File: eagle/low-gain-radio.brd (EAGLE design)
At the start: 99 x 100 mm, 109 parts, among them Y1 32MHz

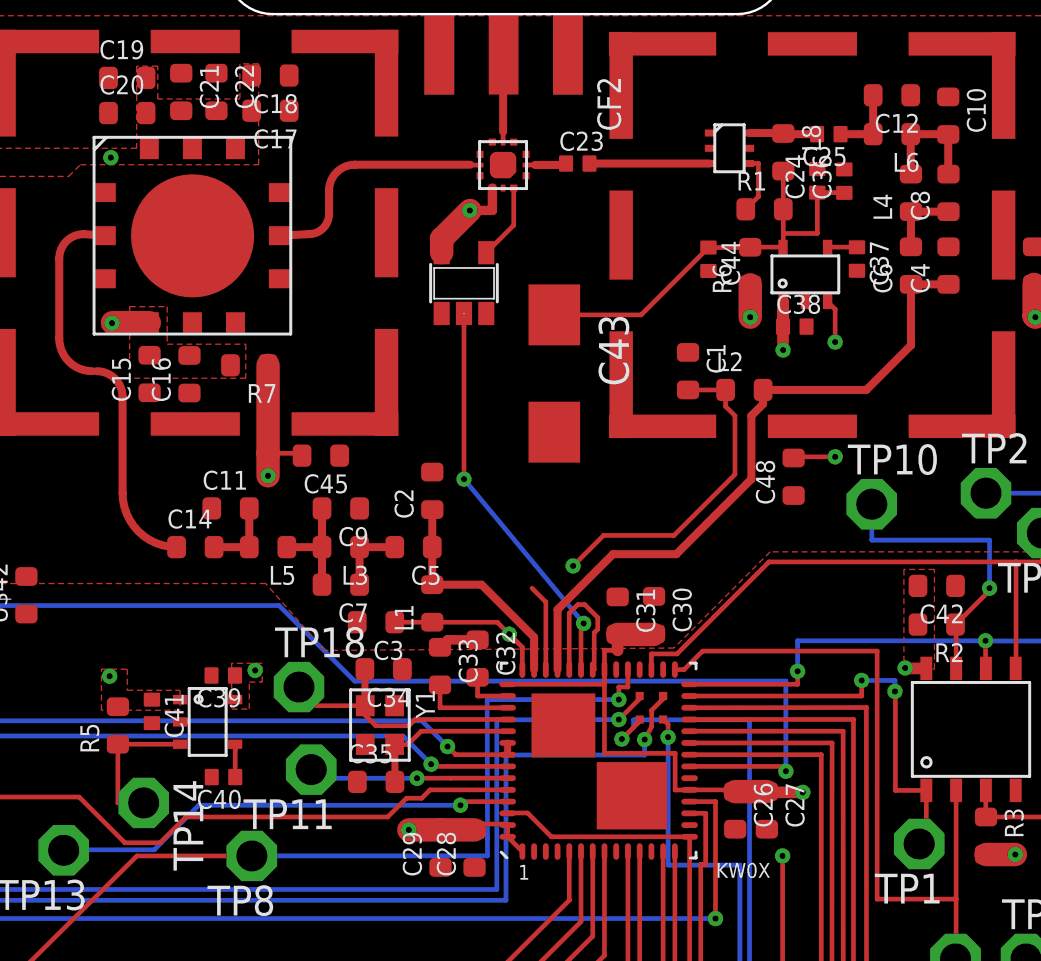
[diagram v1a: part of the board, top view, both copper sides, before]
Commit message: Fixed some part sizes. I'm not gonna talk about it since Andrew will surely fire me.
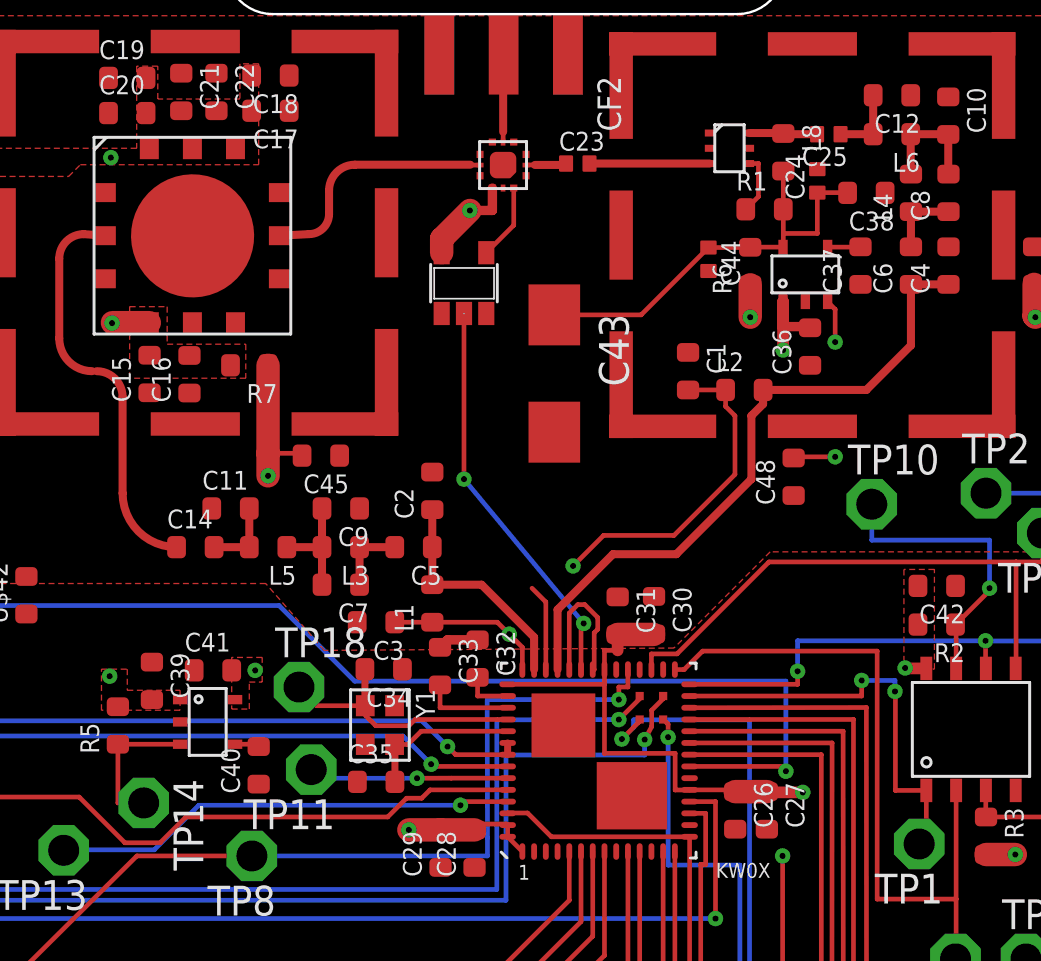
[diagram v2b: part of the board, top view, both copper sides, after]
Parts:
- C36, C39: value 2.2uF -> 1uF; device rcl_custom:.0402-B-NOSILK -> rcl_custom:.0603-B-NOSILK
- C37, C40: device rcl_custom:.0402-B-NOSILK -> rcl_custom:.0603-B-NOSILK
- C38: value 1uF -> 2.2nF; device rcl_custom:.0402-B-NOSILK -> rcl_custom:.0603-B-NOSILK
- C41: value 1uF -> 2.2uF; device rcl_custom:.0402-B-NOSILK -> rcl_custom:.0603-B-NOSILK
- moved C36 7.20 mm to (85.1, 76.0)
- moved C38 6.46 mm to (87.5, 82.5), turned to 180 degrees
- moved C41 3.13 mm to (59.6, 62.1), turned to 0 degrees
- moved C39 3.05 mm to (57.0, 61.7), turned to 270 degrees
- moved C40 1.58 mm to (61.6, 58.1), turned to 90 degrees
- moved C37 0.32 mm to (87.2, 79.4), turned to 90 degrees
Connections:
- net 3.3V: now also C41.2; no longer C39.1
- net GND: now also C36.1, C37.1, C38.1, C39.1, C40.1, C41.1; no longer C36.2, C37.2, C38.2, C39.2, C40.2, C41.2
- net N$1: now also C37.2; no longer C37.1
- net N$13: now also C40.2; no longer C40.1
- net V+: now also C36.2, C39.2; no longer C38.1, C41.1
- net VBIAS: now also C38.2; no longer C36.1
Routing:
- net V+: track 126.4 -> 127.6 mm
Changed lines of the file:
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@@
 <element name="C13" library="rcl_custom" package=".0603-B-NOSILK" value="10uF" x="45.65" y="81.85" rot="R180"/>
 <element name="C46" library="rcl_custom" package=".0603-B-NOSILK" value="10uF" x="48.8" y="84.6" rot="R270"/>
-<element name="C36" library="rcl_custom" package=".0402-B-NOSILK" value="2.2uF" x="86.56" y="83" rot="R90"/>
-<element name="C37" library="rcl_custom" package=".0402-B-NOSILK" value="10nF" x="87.1" y="79.68" rot="R270"/>
-<element name="C38" library="rcl_custom" package=".0402-B-NOSILK" value="1uF" x="84.45" y="76.8"/>
 <element name="U$8" library="psas_c3_team05" package="AAT3215" value="AAT3215" x="59.4" y="60.05" rot="R90">
 <attribute name="MFN" value="Skyworks" x="59.4" y="60.05" size="1.778" layer="27" rot="R90" display="off"/>
 <attribute name="MFN-PN" value="AAT3215" x="59.4" y="60.05" size="1.778" layer="27" rot="R90" display="off"/>
 </element>
-<element name="C39" library="rcl_custom" package=".0402-B-NOSILK" value="2.2uF" x="60.09" y="61.93" rot="R180"/>
-<element name="C40" library="rcl_custom" package=".0402-B-NOSILK" value="10nF" x="60.1" y="57.6" rot="R180"/>
-<element name="C41" library="rcl_custom" package=".0402-B-NOSILK" value="1uF" x="57.05" y="60.4" rot="R270"/>
 <element name="TP1" library="testpad" package="P1-13" value="TPSPAD1-13" x="89.75" y="54.75" rot="R180">
 <attribute name="TP_SIGNAL_NAME" value="" x="89.75" y="54.75" size="1.778" layer="27" rot="R180" display="off"/>
@@
 <element name="C48" library="rcl_custom" package=".0603-B-NOSILK" value="100nF" x="84.4" y="70.4" rot="R90"/>
 <element name="U$42" library="psas_c3_team05" package=".0603-B-NOSILK" value="742792651" x="51.7" y="65.35" rot="R90"/>
+<element name="C39" library="rcl_custom" package=".0603-B-NOSILK" value="1uF" x="57.05" y="61.7" rot="R270"/>
+<element name="C40" library="rcl_custom" package=".0603-B-NOSILK" value="10nF" x="61.6" y="58.1" rot="R90"/>
+<element name="C41" library="rcl_custom" package=".0603-B-NOSILK" value="2.2uF" x="59.65" y="62.15"/>
+<element name="C36" library="rcl_custom" package=".0603-B-NOSILK" value="1uF" x="85.1" y="75.95" rot="R90"/>
+<element name="C37" library="rcl_custom" package=".0603-B-NOSILK" value="10nF" x="87.25" y="79.4" rot="R90"/>
+<element name="C38" library="rcl_custom" package=".0603-B-NOSILK" value="2.2nF" x="87.5" y="82.5" rot="R180"/>
 </elements>
 <signals>
@@
 <contactref element="C29" pad="1"/>
 <contactref element="U$8" pad="2"/>
-<contactref element="C41" pad="2"/>
-<contactref element="C39" pad="2"/>
-<contactref element="C40" pad="2"/>
 <contactref element="U$1" pad="4"/>
 <contactref element="TRSWITCH" pad="11"/>
 <contactref element="U$7" pad="2"/>
-<contactref element="C38" pad="2"/>
-<contactref element="C36" pad="2"/>
-<contactref element="C37" pad="2"/>
 <contactref element="C42" pad="1"/>
 <contactref element="KW0X" pad="2"/>
@@
 <contactref element="LED3" pad="K"/>
 <contactref element="U$42" pad="1"/>
-<wire x1="87.1" y1="79.18" x2="86.56" y2="83.5" width="0" layer="19" extent="1-1"/>
-<wire x1="84.899" y1="77.858" x2="87.1" y2="79.18" width="0" layer="19" extent="1-1"/>
-<wire x1="84.95" y1="76.8" x2="84.899" y2="77.858" width="0" layer="19" extent="1-1"/>
-<wire x1="80.8275" y1="85.05" x2="86.56" y2="83.5" width="0" layer="19" extent="1-1"/>
-<wire x1="84.4" y1="69.6" x2="84.95" y2="76.8" width="0" layer="19" extent="1-1"/>
+<contactref element="C39" pad="1"/>
+<contactref element="C40" pad="1"/>
+<contactref element="C41" pad="1"/>
+<contactref element="C36" pad="1"/>
+<contactref element="C37" pad="1"/>
+<contactref element="C38" pad="1"/>
+<wire x1="87.25" y1="78.6" x2="88.3" y2="82.5" width="0" layer="19" extent="1-1"/>
+<wire x1="84.899" y1="77.858" x2="87.25" y2="78.6" width="0" layer="19" extent="1-1"/>
+<wire x1="85.1" y1="75.15" x2="84.899" y2="77.858" width="0" layer="19" extent="1-1"/>
+<wire x1="84.4" y1="69.6" x2="85.1" y2="75.15" width="0" layer="19" extent="1-1"/>
+<wire x1="80.8275" y1="85.05" x2="88.3" y2="82.5" width="0" layer="19" extent="1-1"/>
 <wire x1="91.3" y1="65.75" x2="84.4" y2="69.6" width="0" layer="19" extent="1-1"/>
 <wire x1="93.865" y1="57.032" x2="91.3" y2="65.75" width="0" layer="19" extent="1-1"/>
-<wire x1="57.05" y1="59.9" x2="58.258" y2="59.951" width="0" layer="19" extent="1-1"/>
+<wire x1="58.258" y1="59.951" x2="58.85" y2="62.15" width="0" layer="19" extent="1-1"/>
 <wire x1="69.35" y1="53.75" x2="65.8079125" y2="57.39725625" width="0" layer="19" extent="1-1"/>
 <wire x1="73.338371875" y1="54.427225" x2="70.8" y2="53.75" width="0" layer="19" extent="1-1"/>
@@
 <contactref element="U$9" pad="6"/>
 <contactref element="C13" pad="2"/>
-<contactref element="C38" pad="1"/>
-<contactref element="C41" pad="1"/>
 <contactref element="U$8" pad="1"/>
 <contactref element="U$7" pad="1"/>
@@
 <via x="44.85" y="80.45" extent="1-16" drill="0.254"/>
 <wire x1="83.949" y1="77.858" x2="83.949" y2="76.801" width="0.5" layer="1"/>
-<wire x1="83.949" y1="76.801" x2="83.95" y2="76.8" width="0.5" layer="1"/>
-<wire x1="83.949" y1="77.858" x2="83.949" y2="75.801" width="0.5" layer="1"/>
+<wire x1="83.949" y1="77.858" x2="83.949" y2="76.8" width="0.5" layer="1"/>
+<wire x1="83.949" y1="76.8" x2="83.949" y2="75.801" width="0.5" layer="1"/>
 <wire x1="83.949" y1="75.801" x2="83.95" y2="75.8" width="0.5" layer="1"/>
 <via x="83.95" y="75.8" extent="1-16" drill="0.254"/>
@@
 <wire x1="57.95" y1="71.9" x2="57.95" y2="70.85" width="1" layer="15"/>
 <wire x1="57.95" y1="70.85" x2="58.05" y2="70.85" width="1" layer="15"/>
+<contactref element="C39" pad="2"/>
+<contactref element="C36" pad="2"/>
+<wire x1="85.1" y1="76.75" x2="85.1" y2="76.8" width="0.2" layer="1"/>
+<wire x1="85.1" y1="76.8" x2="83.949" y2="76.8" width="0.4" layer="1"/>
 </signal>
 <signal name="SWD_DIO">
@@
 <contactref element="R2" pad="2"/>
 <contactref element="U$8" pad="5"/>
-<contactref element="C39" pad="1"/>
 <contactref element="R3" pad="2"/>
 <contactref element="R8" pad="2"/>
@@
 <via x="68" y="55.35" extent="1-16" drill="0.254"/>
 <polygon width="0.2" layer="1" thermals="no">
-<vertex x="60.45" y="62.45"/>
+<vertex x="60.45" y="62.7"/>
 <vertex x="60.45" y="60.5"/>
 <vertex x="61.2" y="60.5"/>
 <vertex x="61.2" y="61.65"/>
 <vertex x="61.75" y="61.65"/>
-<vertex x="61.75" y="62.45"/>
+<vertex x="61.75" y="62.7"/>
 </polygon>
 <via x="61.45" y="62.15" extent="1-16" drill="0.254"/>
@@
 <wire x1="72.165596875" y1="55.6" x2="71.05" y2="55.6" width="0.2" layer="1"/>
 <wire x1="71.05" y1="55.6" x2="70.8" y2="55.35" width="0.2" layer="1"/>
+<contactref element="C41" pad="2"/>
 </signal>
 <signal name="N$7">
@@
 </signal>
 <signal name="N$1">
-<contactref element="C37" pad="1"/>
 <contactref element="U$7" pad="4"/>
 <wire x1="85.849" y1="80.188" x2="87.1" y2="80.188" width="0.2" layer="1"/>
-<wire x1="87.1" y1="80.188" x2="87.1" y2="80.18" width="0.2" layer="1"/>
+<contactref element="C37" pad="2"/>
+<wire x1="87.1" y1="80.188" x2="87.25" y2="80.2" width="0" layer="19" extent="1-1"/>
 </signal>
 <signal name="PA_EN">
@@
 <signal name="N$13">
 <contactref element="U$8" pad="4"/>
-<contactref element="C40" pad="1"/>
-<wire x1="60.588" y1="59.001" x2="60.6" y2="58.775" width="0.2" layer="1"/>
-<wire x1="60.6" y1="58.775" x2="60.6" y2="57.6" width="0.2" layer="1"/>
+<contactref element="C40" pad="2"/>
+<wire x1="60.588" y1="59.001" x2="61.5" y2="59.001" width="0.2" layer="1"/>
+<wire x1="61.5" y1="59.001" x2="61.6" y2="58.9" width="0.4064" layer="1"/>
 </signal>
 <signal name="VBIAS">
 <contactref element="R1" pad="2"/>
-<contactref element="C36" pad="1"/>
 <contactref element="C24" pad="1"/>
 <contactref element="C43" pad="+"/>
@@
 <wire x1="83.96" y1="80.77" x2="83.96" y2="81.8" width="0.2" layer="1"/>
 <wire x1="83.96" y1="81.8" x2="83.96" y2="83.43" width="0.2" layer="1"/>
-<wire x1="85.41" y1="82.51" x2="86.56" y2="82.51" width="0.2" layer="1"/>
-<wire x1="86.56" y1="82.51" x2="86.56" y2="82.5" width="0.2" layer="1"/>
 <wire x1="85.41" y1="82.51" x2="85.41" y2="80.77" width="0.2" layer="1"/>
 <wire x1="85.41" y1="80.77" x2="83.96" y2="80.77" width="0.2" layer="1"/>
@@
 <wire x1="74.2" y1="77.3" x2="77.9" y2="77.3" width="0.2" layer="1"/>
 <wire x1="77.9" y1="77.3" x2="80.77" y2="80.17" width="0.2" layer="1"/>
+<contactref element="C38" pad="2"/>
+<wire x1="86.56" y1="82.51" x2="85.4" y2="82.51" width="0.2" layer="1"/>
+<wire x1="85.4" y1="82.51" x2="85.4" y2="82.5" width="0.2" layer="1"/>
+<wire x1="86.7" y1="82.5" x2="86.7" y2="82.51" width="0.4" layer="1"/>
+<wire x1="86.7" y1="82.51" x2="86.56" y2="82.51" width="0.4" layer="1"/>
+<wire x1="85.41" y1="82.51" x2="85.4" y2="82.51" width="0" layer="19" extent="1-1"/>
 </signal>
 <signal name="PTE0">

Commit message: Updated passive components with attributes for BOM
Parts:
- C38: value 2.2nF -> 2.2uF

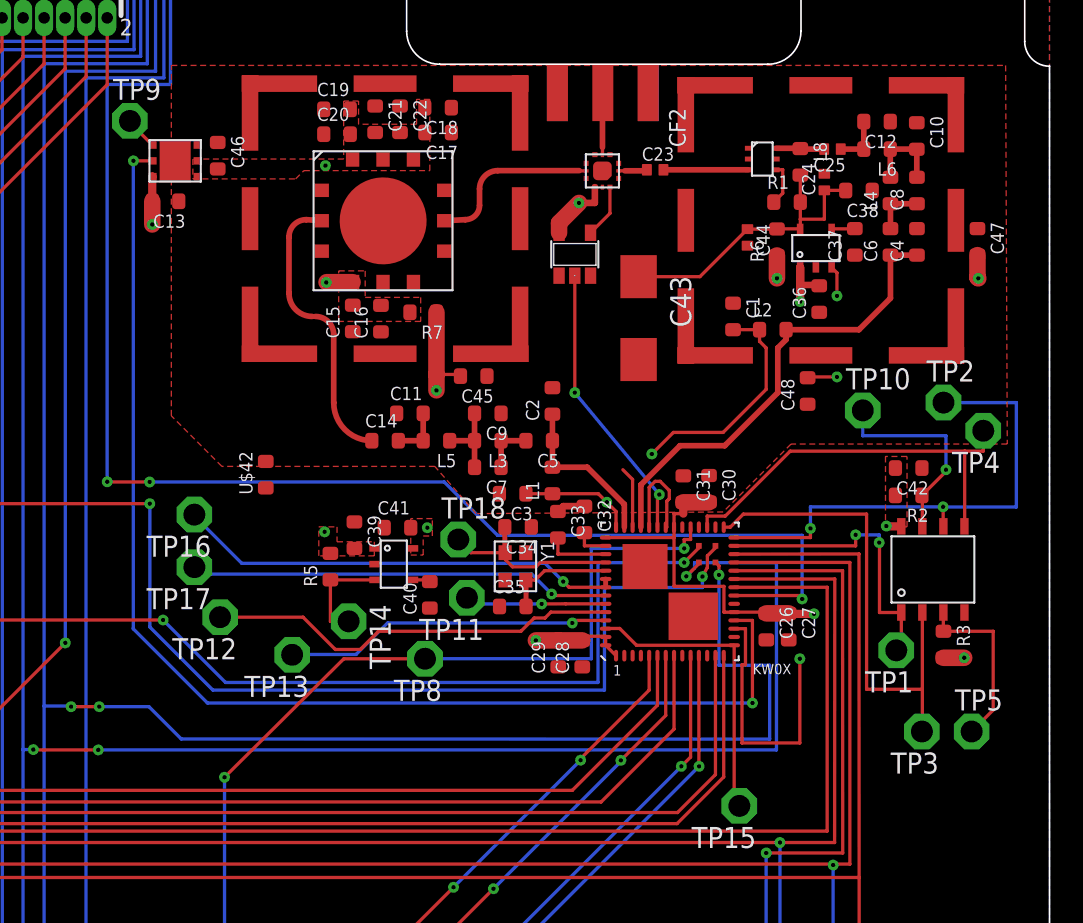
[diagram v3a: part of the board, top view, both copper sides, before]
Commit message: Added test point names, fixed some ugly traces
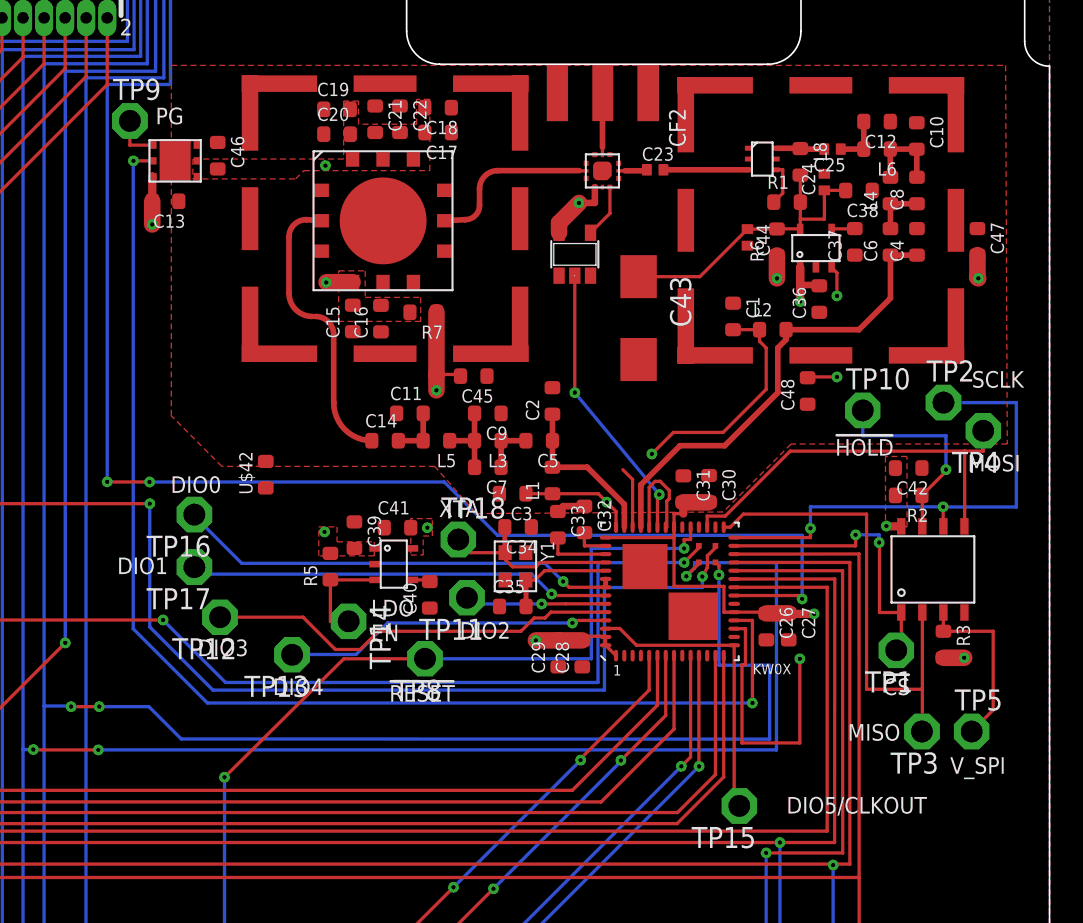
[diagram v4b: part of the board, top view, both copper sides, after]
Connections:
- net N$11 renamed V_SPI
- net N$12 renamed LDO_EN
- net N$3 renamed DIO2
- net N$5 renamed DIO3
- net N$6 renamed XTA
- net N$9 renamed DIO4
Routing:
- net N$4: track 2.03 -> 2.92 mm
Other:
- board text added: "!CS"
- board text added: "!HOLD"
- board text added: "!RESET"
- board text added: "DIO0"
- board text added: "DIO1"
- board text added: "DIO2"
- board text added: "DIO3"
- board text added: "DIO4"
- board text added: "DIO5/CLKOUT"
- board text added: "LDO EN"
- board text added: "MISO"
- board text added: "MOSI"
- board text added: "PG"
- board text added: "SCLK"
- board text added: "V_SPI"
- board text added: "XTA"
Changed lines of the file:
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@@
 <wire x1="49.85" y1="71.25" x2="59.75" y2="71.25" width="0.2" layer="100" style="shortdash"/>
 <text x="49.65" y="90.35" size="0.75" layer="100">Cut power plane to here</text>
+<text x="62.15" y="62.8" size="1" layer="21" font="vector" ratio="16">XTA</text>
+<text x="97.45" y="71.6" size="1" layer="21" font="vector" ratio="16" rot="R180">SCLK</text>
+<text x="89.6" y="67.5" size="1" layer="21" font="vector" ratio="16" rot="R180">!HOLD</text>
+<text x="97.25" y="66.55" size="1" layer="21" font="vector" ratio="16" rot="R180">MOSI</text>
+<text x="90" y="50.3" size="1" layer="21" font="vector" ratio="16" rot="R180">MISO</text>
+<text x="93" y="47.3" size="1" layer="21" font="vector" ratio="16">V_SPI</text>
+<text x="91.6" y="45.9" size="1" layer="21" font="vector" ratio="16" rot="R180">DIO5/CLKOUT</text>
+<text x="59.15" y="51.65" size="1" layer="21" font="vector" ratio="16">!RESET</text>
+<text x="58.05" y="55.3" size="1" layer="21" font="vector" ratio="16">LDO
+EN</text>
+<text x="88.95" y="52.05" size="1" layer="21" font="vector" ratio="16">!CS</text>
+<text x="45.95" y="64.25" size="1" layer="21" font="vector" ratio="16">DIO0</text>
+<text x="45.8" y="60.35" size="1" layer="21" font="vector" ratio="16" rot="R180">DIO1</text>
+<text x="63.4" y="55.45" size="1" layer="21" font="vector" ratio="16">DIO2</text>
+<text x="50.65" y="55.4" size="1" layer="21" font="vector" ratio="16" rot="R180">DIO3</text>
+<text x="55.2" y="53.05" size="1" layer="21" font="vector" ratio="16" rot="R180">DIO4</text>
+<text x="45.05" y="86.5" size="1" layer="21" font="vector" ratio="16">PG</text>
 </plain>
 <attributes>
@@
 <wire x1="79.966171875" y1="45.673828125" x2="80.28" y2="45.36" width="0.2" layer="1"/>
 </signal>
-<signal name="N$6">
+<signal name="XTA">
 <contactref element="KW0X" pad="46"/>
 <contactref element="C34" pad="2"/>
@@
 <contactref element="U$9" pad="4"/>
 <contactref element="TP9" pad="TP"/>
-<wire x1="44.86434375" y1="85.2391875" x2="43.5" y2="86.60353125" width="0.2" layer="1"/>
 <wire x1="43.5" y1="86.60353125" x2="43.5" y2="86.7" width="0.2" layer="1"/>
+<wire x1="44.86434375" y1="85.2391875" x2="43.5" y2="85.2391875" width="0.2" layer="1"/>
+<wire x1="43.5" y1="85.2391875" x2="43.5" y2="86.7" width="0.2" layer="1"/>
 </signal>
 <signal name="!HOLD">
@@
 <wire x1="37.05" y1="90.6" x2="37.05" y2="48.76" width="0.2" layer="16"/>
 </signal>
-<signal name="N$3">
+<signal name="DIO2">
 <contactref element="KW0X" pad="51"/>
 <contactref element="TP11" pad="TP"/>
@@
 <wire x1="64.21" y1="57.55" x2="63.84" y2="57.92" width="0.2" layer="16"/>
 </signal>
-<signal name="N$5">
+<signal name="DIO3">
 <contactref element="KW0X" pad="52"/>
 <contactref element="TP12" pad="TP"/>
@@
 <wire x1="68.55" y1="56.7" x2="67.9" y2="56.7" width="0.2" layer="1"/>
 </signal>
-<signal name="N$9">
+<signal name="DIO4">
 <contactref element="KW0X" pad="53"/>
 <contactref element="TP13" pad="TP"/>
@@
 <wire x1="47.81" y1="59.35" x2="47.39" y2="59.77" width="0.2" layer="16"/>
 </signal>
-<signal name="N$11">
+<signal name="V_SPI">
 <contactref element="U$1" pad="3"/>
 <contactref element="R3" pad="1"/>
@@
 <wire x1="95.6" y1="51.15" x2="94.3" y2="49.85" width="0.2" layer="1"/>
 </signal>
-<signal name="N$12">
+<signal name="LDO_EN">
 <contactref element="U$8" pad="3"/>
 <contactref element="R5" pad="1"/>
@@
 </board>
 </drawing>
+<compatibility>
+<note version="6.3" minversion="6.2.2" severity="warning">
+Since Version 6.2.2 text objects can contain more than one line,
+which will not be processed correctly with this version.
+</note>
+</compatibility>
 </eagle>
